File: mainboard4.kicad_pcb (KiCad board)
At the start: 4 copper layers, 100 x 100 mm, 238 parts, among them J1 Conn_01x04_Pin, J10 RJMG201K21120FR, J11 690-019-298-412, J12 USB3_A, J13 USB_C_Receptacle_USB2.0_16P, J14 Micro_SD_Card_Det, J2 Conn_01x04_Pin, J3 Bus_M.2_Socket_B, J4 JST_SHBM04B-SRSS-TB, J5 THD-20-R, J6 Conn_02x07_Odd_Even, J7 Bus_M.2_Socket_E, J8 USB_A_Stacked, J9 Barrel_Jack, SW1 Right angle Tact button, SW2 SW_DIP_x04, SW3 SW_Push, U1 74LVC1G07SE-7, U10 MCP2562-E-SN, U11 MCP2562-E-SN, U12 STM32H723VGT6, U13 LAN8742A, U14 JMS578, U15 CAT250xxx, U16 LAN9514, U17 CAT250xxx, U18 RT9742SNGV, U2 BNO086, U3 RT9742GGJ5, U4 ASEK-32.768KHZ-L-R-T, U5 AP64502QSP-13, U6 ASEK-32.768KHZ-L-R-T, U7 AP64502, U8 AP22653W6, U9 CH221K, Y1 32.768khz, Y2 16Mhz, Y3 25Mhz, Y4 30Mhz, Y5 25Mhz

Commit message: fix screen
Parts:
- moved U3 0.85 mm to (129.2, 51.5)
- moved C4 0.25 mm to (127.1, 48.0)
- moved Y1 0.18 mm to (173.1, 54.3)
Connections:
- Module1 pad 90: /CM5_GPIO/+1.8v -> unconnected-(Module1A-+1.8v_(Output)-Pad90)
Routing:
- net GND: track 796.8 -> 798.5 mm, vias 385 -> 394
- net /CM5_GPIO/SD_PWR: track 5.46 -> 4.71 mm
- net /CM5_GPIO/SD_PWR_ON: track 49.1 -> 49.8 mm
- net +3.3V: track 308.0 -> 307.4 mm
- net /Ethernet PHY/RXN: track 26.7 -> 26.1 mm
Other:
- board text added: "USBtoSATA"
- board text removed: "3.0"

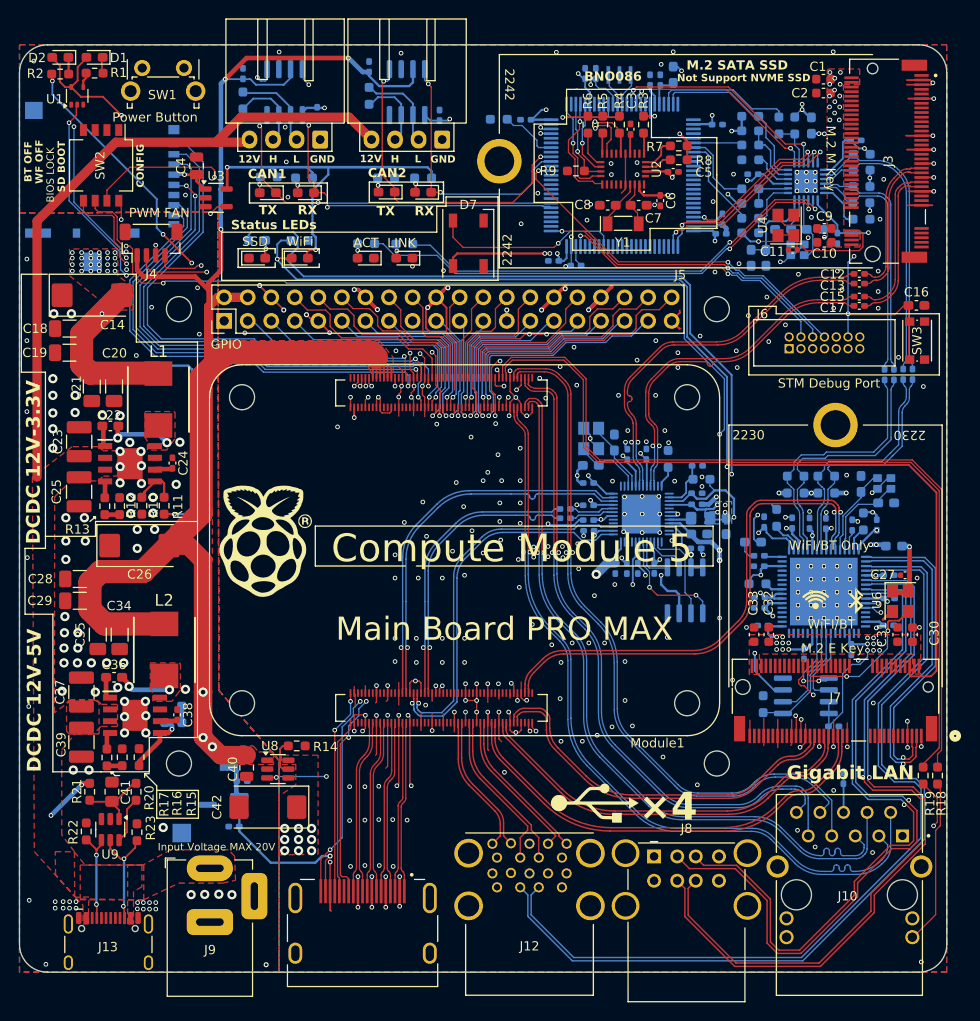
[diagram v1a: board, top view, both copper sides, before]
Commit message: リセットラインのルートを変更
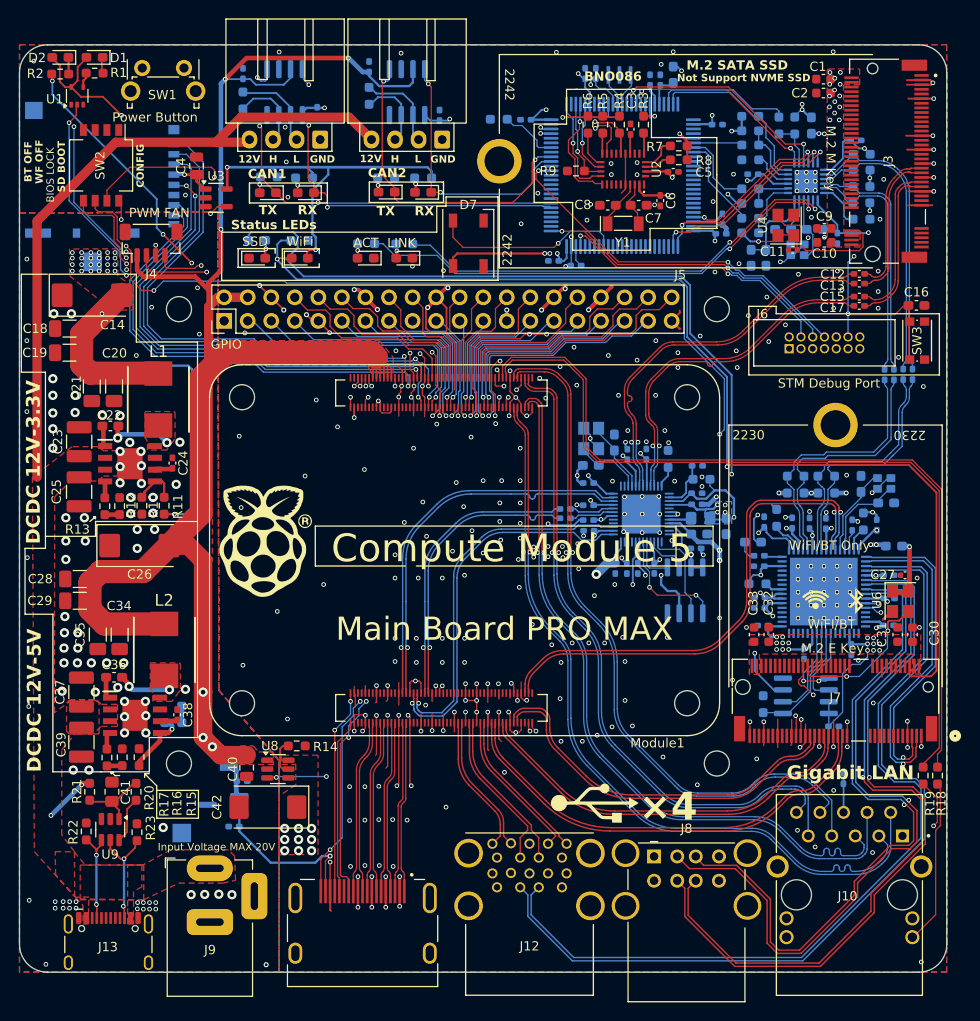
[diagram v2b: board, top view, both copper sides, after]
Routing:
- net /nEXTRST: track 158.1 -> 162.5 mm
- net GND: track 798.5 -> 798.3 mm, vias 394 -> 410
